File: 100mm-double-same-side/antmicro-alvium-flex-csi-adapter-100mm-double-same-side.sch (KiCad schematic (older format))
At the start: 3 parts, among them J1 WE_687622100002_FLEX, J2 WE_687622100002_FLEX, J3 WE_687650100002_FLEX

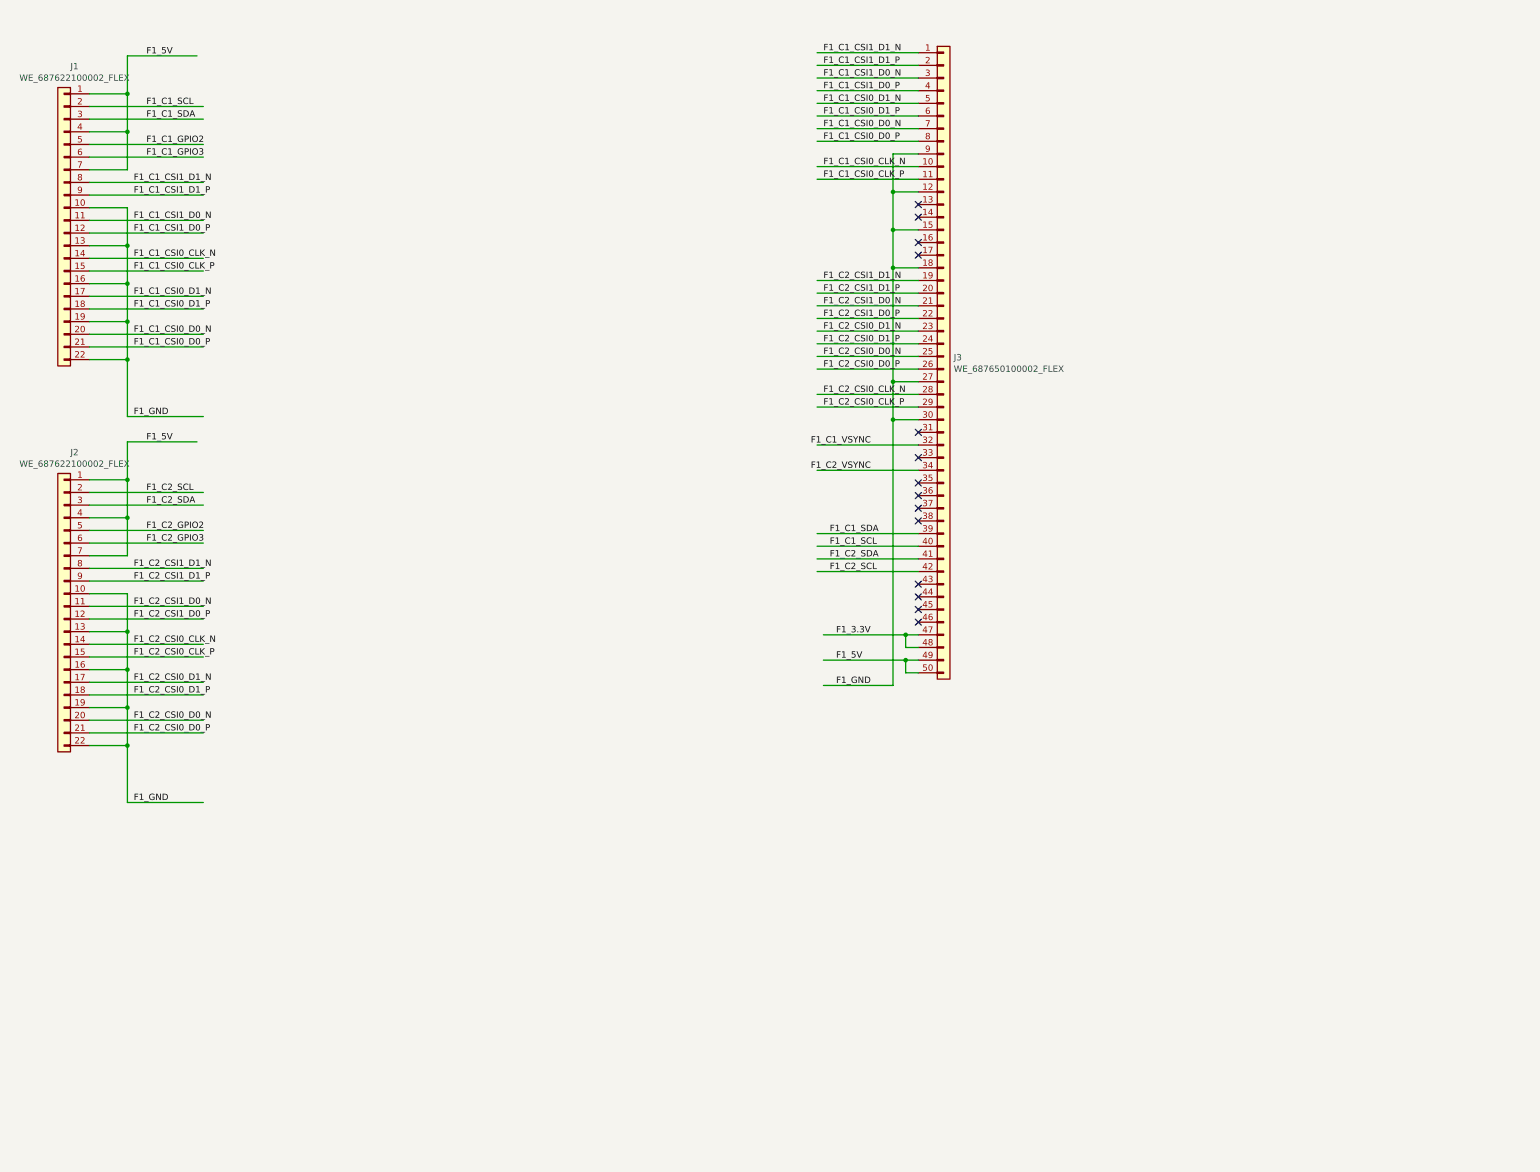
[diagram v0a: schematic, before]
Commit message: 100mm-double-same: Add signage
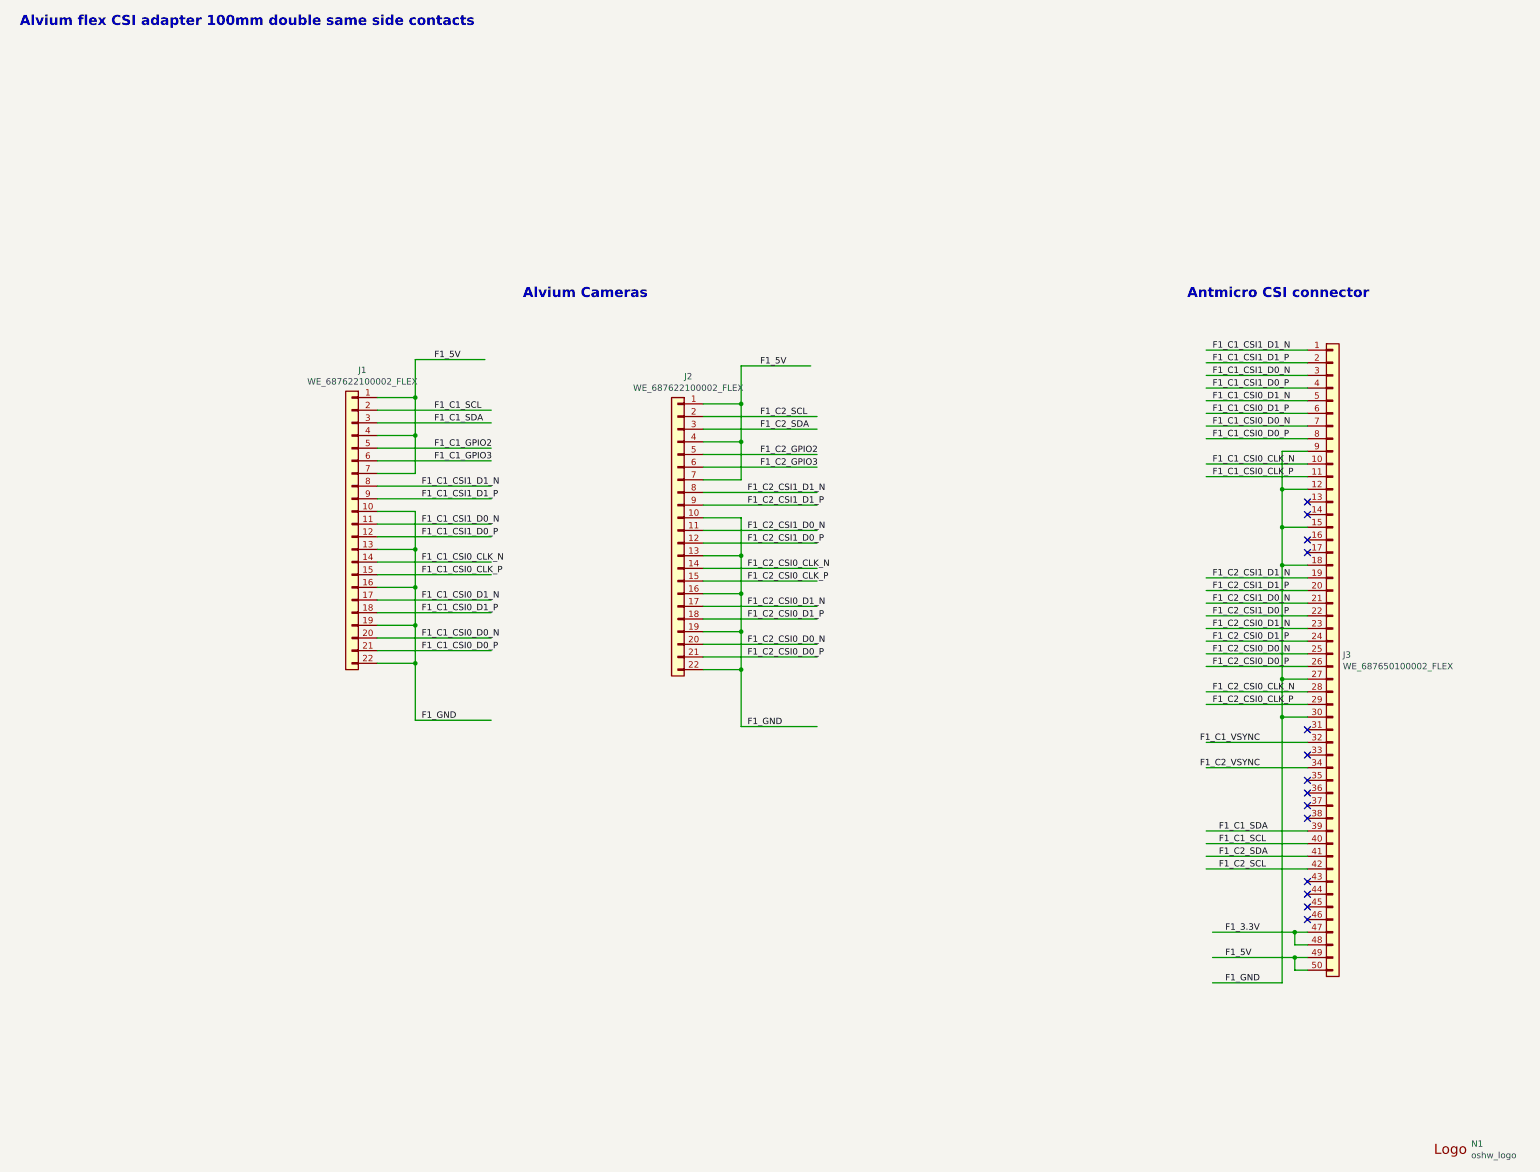
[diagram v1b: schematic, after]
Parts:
- added N1: oshw_logo, antmicro-alvium-flex-csi-adapter-footprints:oshw-logo, symbol antmicro-alvium-flex-csi-adapter:oshw_logo
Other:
- note added: "Alvium Cameras"
- note added: "Alvium flex CSI adapter 100mm double same side contacts"
- note added: "Antmicro CSI connector"
- moved on the sheet: J1, J2, J3

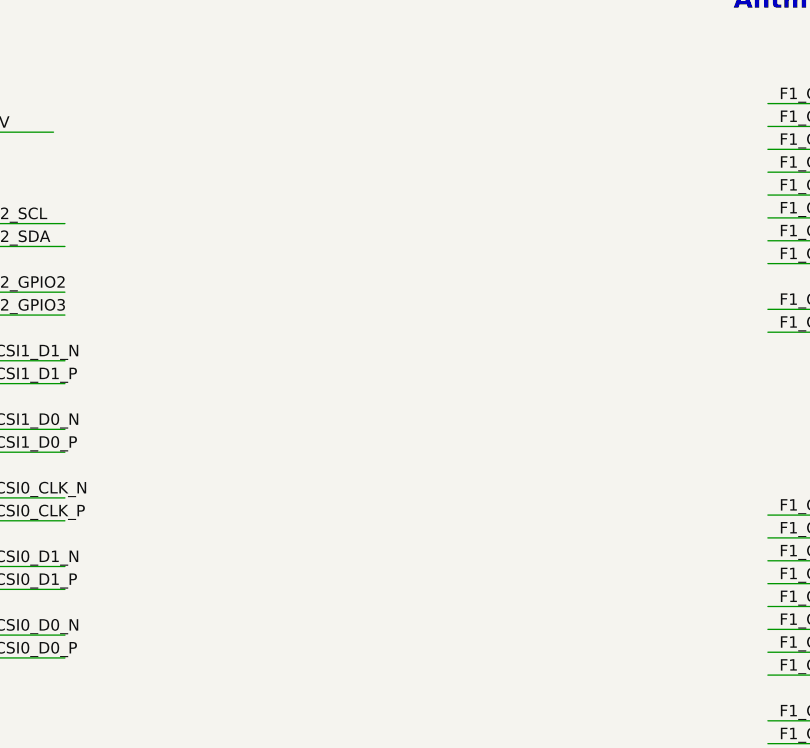
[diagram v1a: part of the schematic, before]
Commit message: Add NMOS transistors for camera triggering in 100mm double same side variant
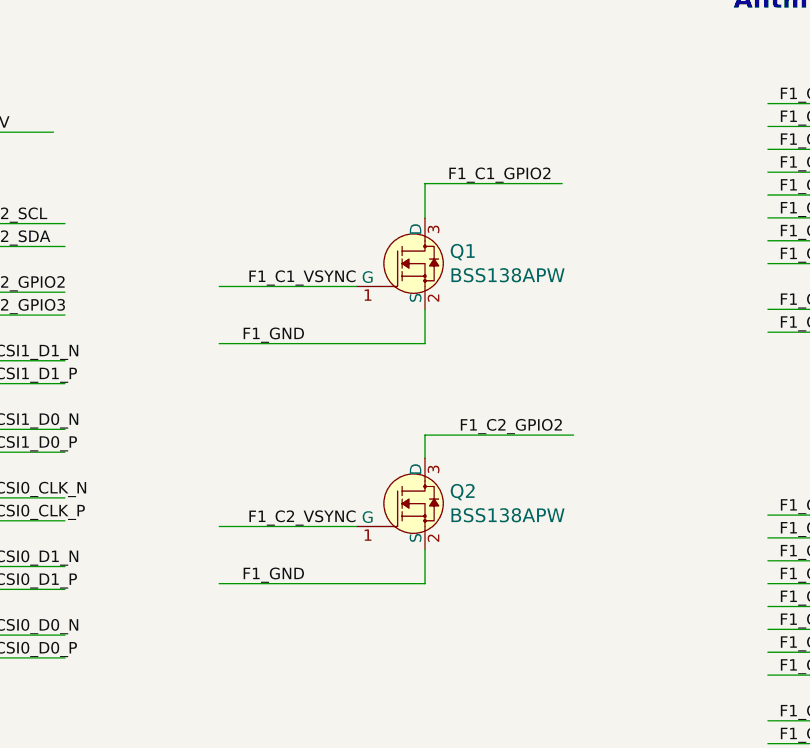
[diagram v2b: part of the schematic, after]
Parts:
- added Q1, Q2: BSS138APW, antmicro-alvium-flex-csi-adapter-footprints:SC70-3, symbol antmicro-alvium-flex-csi-adapter:BSS138APW
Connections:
- wire segments 111 -> 121
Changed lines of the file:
@@
 EndData
 $EndBitmap
+$Comp
+L antmicro-alvium-flex-csi-adapter:BSS138APW Q1
+U 1 1 5F8CC8D0
+P 8500 4100
+F 0 "Q1" H 8608 4153 60  0000 L CNN
+F 1 "BSS138APW" H 8608 4047 60  0000 L CNN
+F 2 "antmicro-alvium-flex-csi-adapter-footprints:SC70-3" H 8700 4300 60  0001 L CNN
+F 3 "" H 8700 4400 60  0001 L CNN
+F 4 "BSS138PW" H 8700 4600 60  0001 L CNN "MPN"
+F 5 "ON Semiconductor" H 8700 5200 60  0001 L CNN "Manufacturer"
+	1    8500 4100
+	1    0    0    -1
+$EndComp
+$Comp
+L antmicro-alvium-flex-csi-adapter:BSS138APW Q2
+U 1 1 5F8CCF32
+P 8500 5150
+F 0 "Q2" H 8608 5203 60  0000 L CNN
+F 1 "BSS138APW" H 8608 5097 60  0000 L CNN
+F 2 "antmicro-alvium-flex-csi-adapter-footprints:SC70-3" H 8700 5350 60  0001 L CNN
+F 3 "" H 8700 5450 60  0001 L CNN
+F 4 "BSS138PW" H 8700 5650 60  0001 L CNN "MPN"
+F 5 "ON Semiconductor" H 8700 6250 60  0001 L CNN "Manufacturer"
+	1    8500 5150
+	1    0    0    -1
+$EndComp
+Wire Wire Line
+	8500 4300 8500 4450
+Wire Wire Line
+	8500 4450 7600 4450
+Wire Wire Line
+	8500 5350 8500 5500
+Wire Wire Line
+	8500 5500 7600 5500
+Wire Wire Line
+	8200 5250 7600 5250
+Wire Wire Line
+	8200 4200 7600 4200
+Wire Wire Line
+	8500 3900 8500 3750
+Wire Wire Line
+	8500 3750 9100 3750
+Wire Wire Line
+	8500 4950 8500 4850
+Wire Wire Line
+	8500 4850 9150 4850
+Text Label 7700 5500 0    50   ~ 0
+F1_GND
+Text Label 7700 4450 0    50   ~ 0
+F1_GND
+Text Label 8200 4200 2    50   ~ 0
+F1_C1_VSYNC
+Text Label 8200 5250 2    50   ~ 0
+F1_C2_VSYNC
+Text Label 8600 3750 0    50   ~ 0
+F1_C1_GPIO2
+Text Label 8650 4850 0    50   ~ 0
+F1_C2_GPIO2
 $EndSCHEMATC
